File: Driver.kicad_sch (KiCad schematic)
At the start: 41 parts, among them U3 IS31FL3741A

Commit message: Schematic done, partially routed
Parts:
- removed R21, R22, R23, R24, R25, R26, R27, R28, R29, R30, R31, R32, R33, R34, R35, R36, R37, R38, R39, R40, R41, R42, R43, R44, R45: 20, symbol Device:R_US
- removed U3: IS31FL3741A, symbol LEDMatrix:IS31FL3741A
- added U3: IS31FL3729-QFLS4-TR, Package_DFN_QFN:Texas_RSN_WQFN-32-1EP_4x4mm_P0.4mm_EP2.8x2.8mm_ThermalVias, symbol LEDMatrix:IS31FL3729
- C17, C19, C21: footprint (none) -> Capacitor_SMD:C_0402_1005Metric; Digikey (none) -> 1276-1445-1-ND; LCSC (none) -> C52923
- C18, C20, C22: footprint (none) -> Capacitor_SMD:C_0402_1005Metric; Digikey (none) -> 1276-1001-1-ND; LCSC (none) -> C1525
- R12: value 100k -> 18k; footprint (none) -> Resistor_SMD:R_0402_1005Metric
- R13, R14, R15, R16, R17, R18, R19, R20: footprint (none) -> Resistor_SMD:R_0402_1005Metric
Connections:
- net +5V: now also U3.23 (PVCC)
- net GND: now also U3.24 (GND), U3.28 (ADDR), U3.9 (GND), U3.PAD (GND)
- net LED_SW0: now also U3.22 (SW1)
- net LED_SW1: now also U3.21 (SW2)
- net LED_SW2: now also U3.20 (SW3)
- net LED_SW3: now also U3.19 (SW4)
- net LED_SW4: now also U3.18 (SW5)
- net LED_SW5: now also U3.17 (SW6)
- net LED_SW6: now also U3.16 (SW7)
- net LED_SW7: now also U3.15 (SW8)
- net LED_SW8: now also U3.14 (SW9/CS16)
- net SCL: now also U3.27 (SCL)
- net SDA: now also U3.26 (SDA)
- net SDB: now also U3.29 (SDB)
- net at R12.1: now also U3.25 (ISET)
- net at R18.1: now also U3.3 (CS6)
- net at R20.1: now also U3.5 (CS8)
- net at R13.1: now also U3.30 (CS1)
- net at R16.1: now also U3.1 (CS4)
- net at R17.1: now also U3.2 (CS5)
- net at R14.1: now also U3.31 (CS2)
- net at R15.1: now also U3.32 (CS3)
- net at R19.1: now also U3.4 (CS7)
- no-connect marks 6 -> 7
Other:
- moved on the sheet: R12

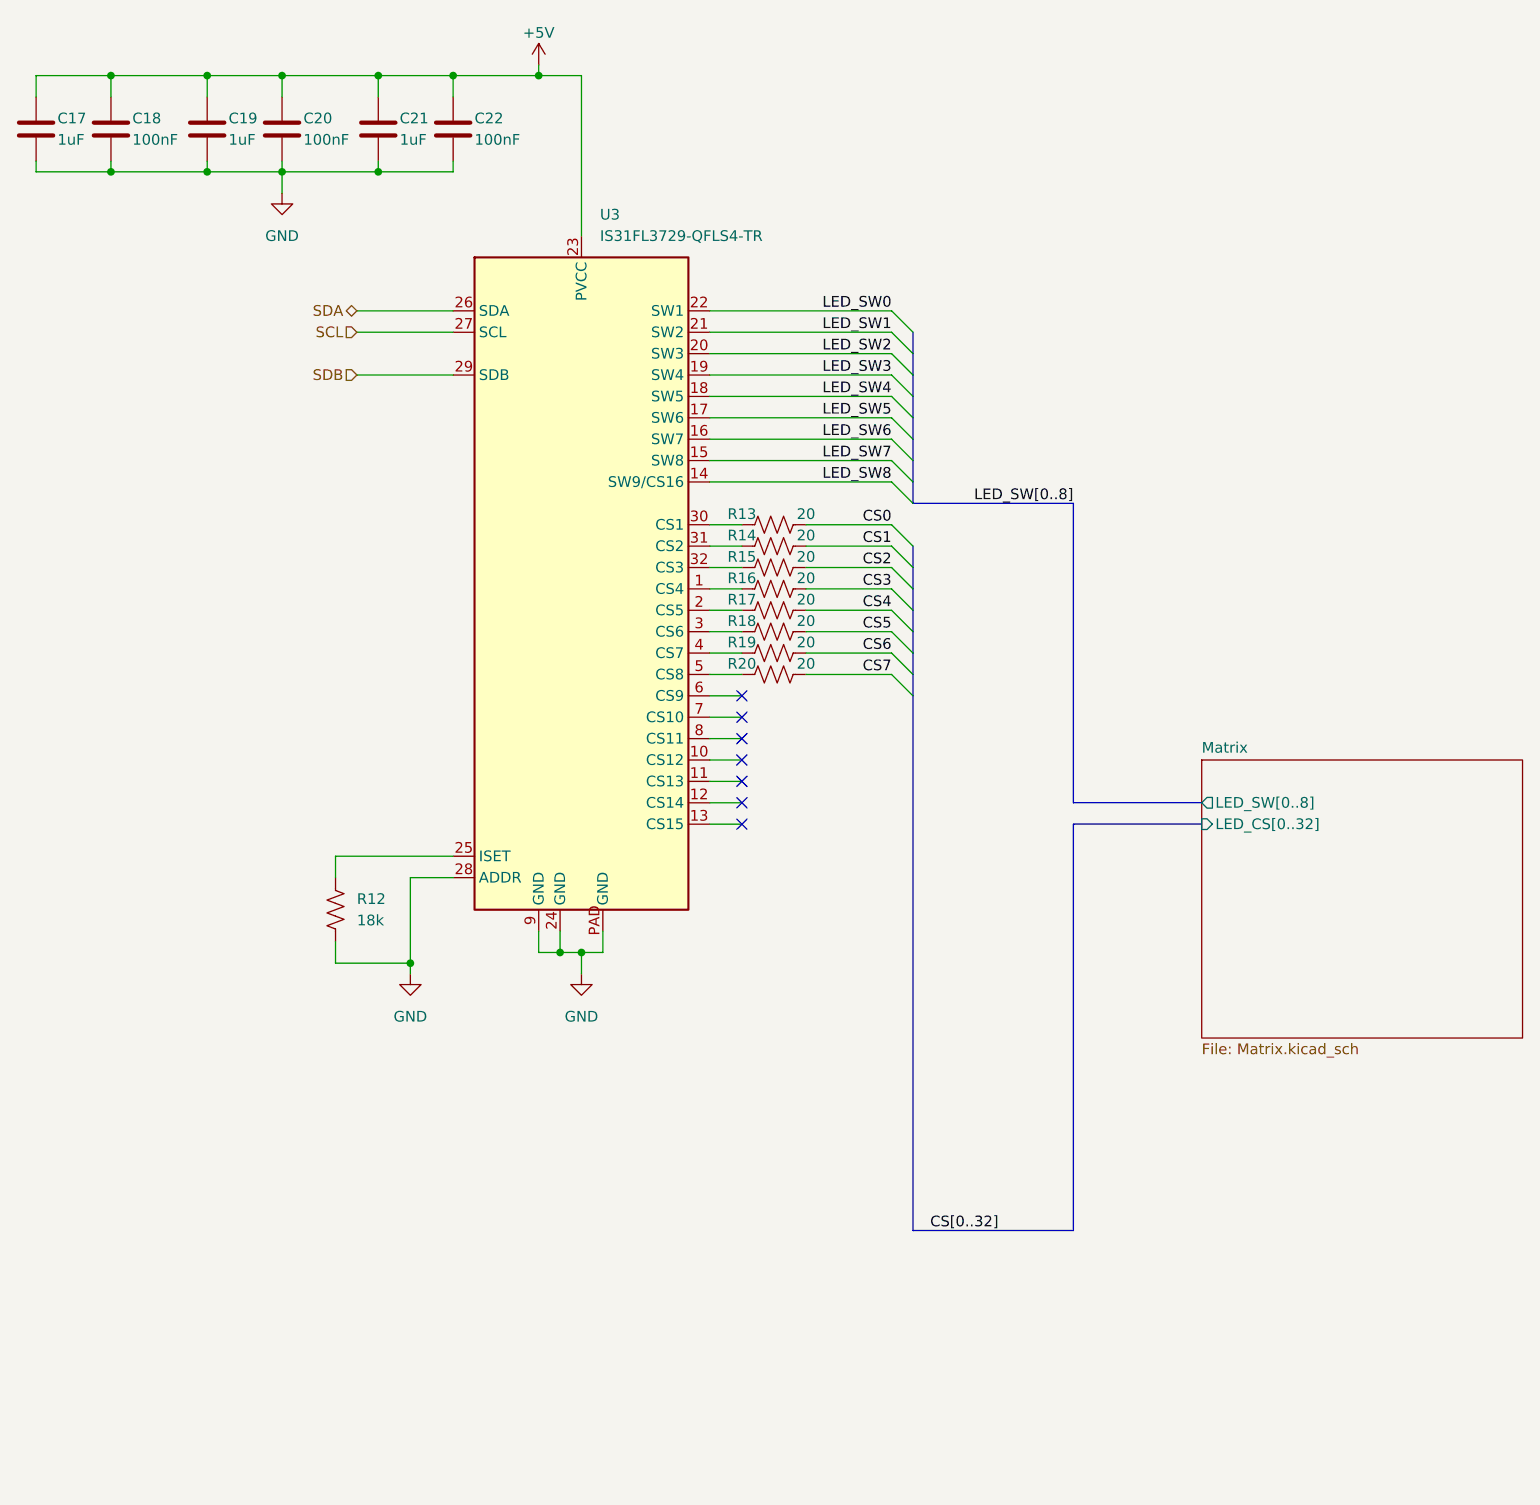
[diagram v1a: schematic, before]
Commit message: Routing complete but not DRC clean
Also want to add 3-9 neopixels here to backlight the legend.
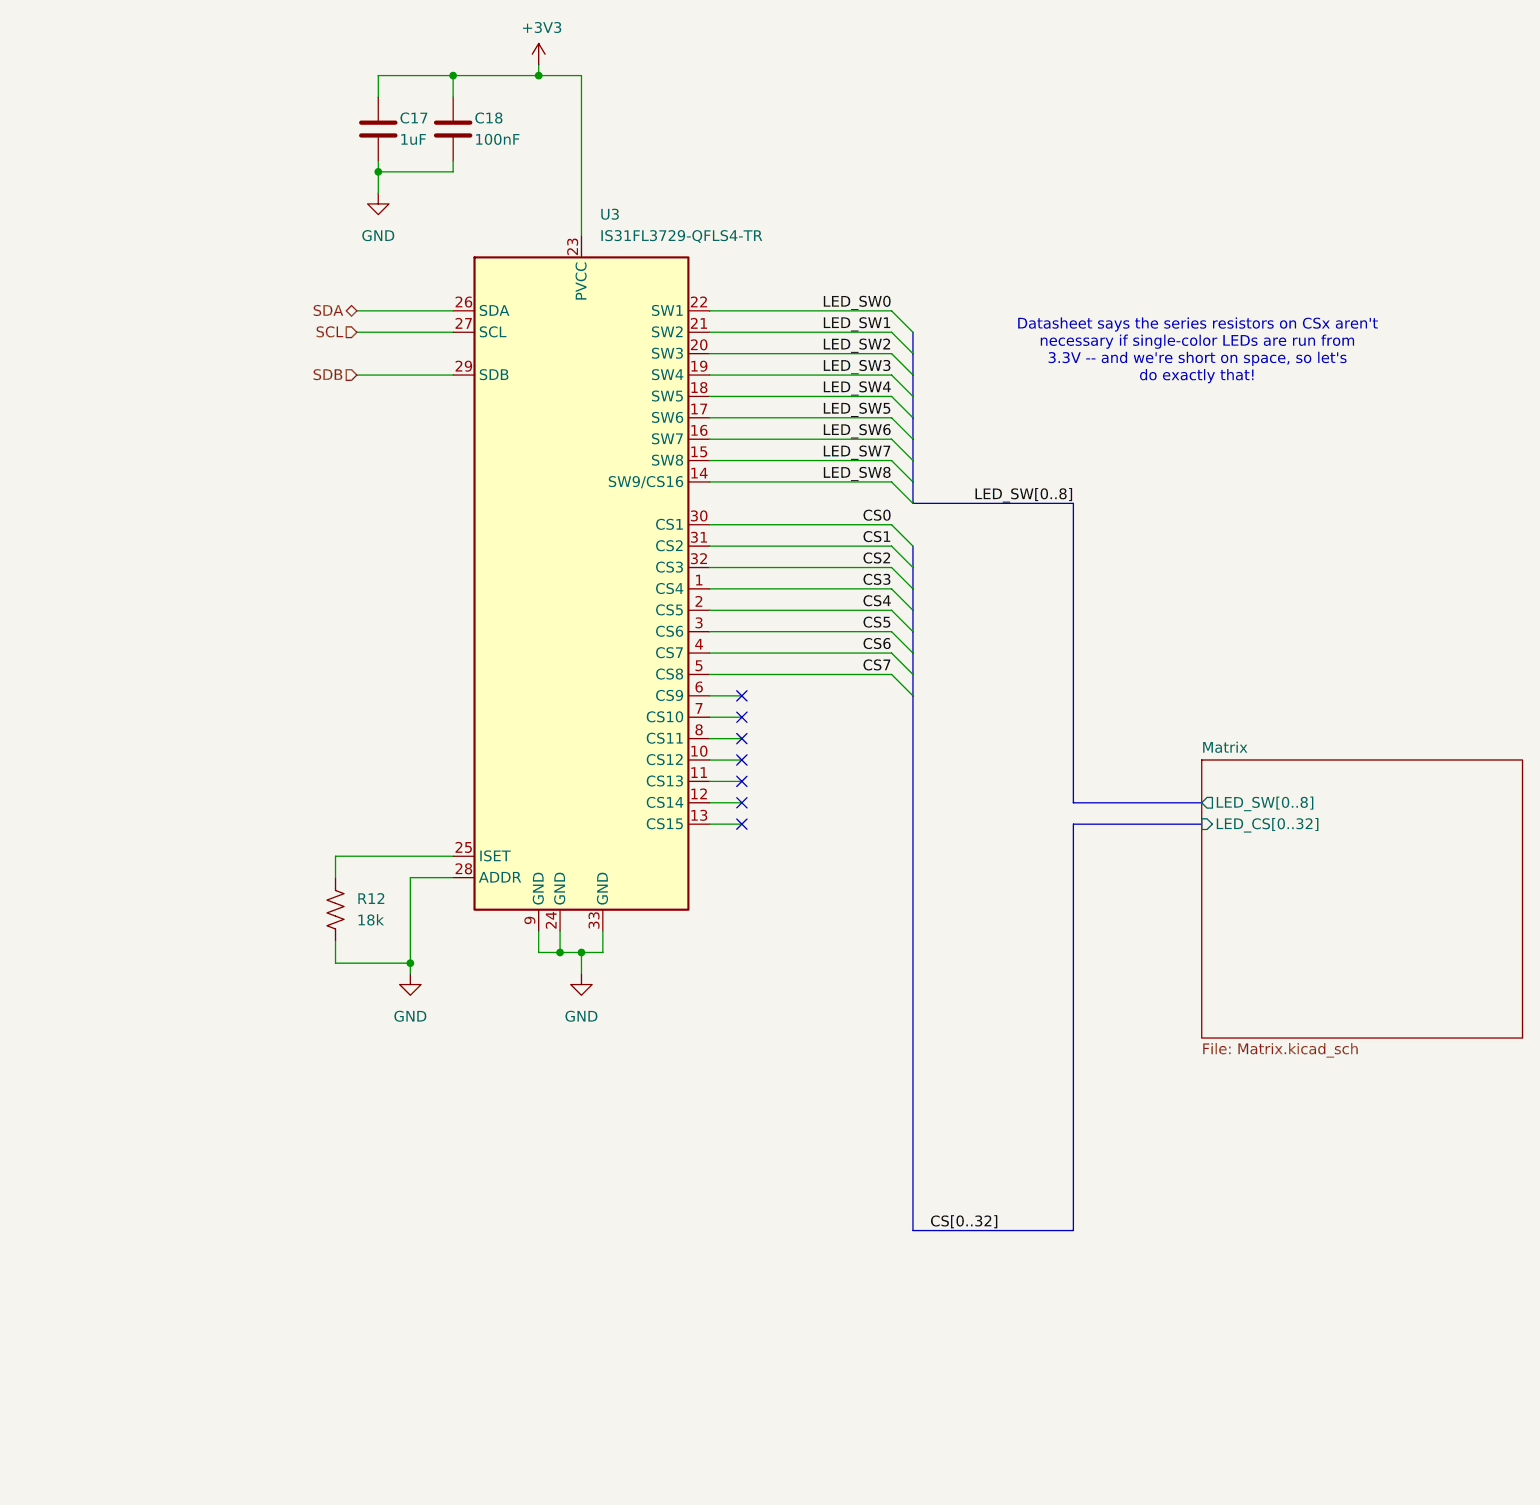
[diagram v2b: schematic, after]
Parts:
- removed C19, C21: 1uF, Capacitor_SMD:C_0402_1005Metric, symbol Device:C
- removed C20, C22: 100nF, Capacitor_SMD:C_0402_1005Metric, symbol Device:C
- removed R13, R14, R15, R16, R17, R18, R19, R20: 20, Resistor_SMD:R_0402_1005Metric, symbol Device:R_US
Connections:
- net CS0: now also U3.30 (CS1)
- net CS1: now also U3.31 (CS2)
- net CS2: now also U3.32 (CS3)
- net CS3: now also U3.1 (CS4)
- net CS4: now also U3.2 (CS5)
- net CS5: now also U3.3 (CS6)
- net CS6: now also U3.4 (CS7)
- net CS7: now also U3.5 (CS8)
- net GND: now also U3.33 (GND); no longer U3.PAD (GND)
- net +5V renamed +3V3
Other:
- note added: "Datasheet says the series resistors on CSx aren't necessary if single-color LEDs are run from 3.3V -- and we're short on space, so let's do exactly that!"
- moved on the sheet: C17, C18

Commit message: Finished version w/ legend on silkscreen, DRC clean
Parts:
- R12: LCSC (none) -> C25762
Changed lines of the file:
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@@
+			)
+		)
+		(property "LCSC" "C25762"
+			(at 57.15 120.65 0)
+			(effects
+				(font
+					(size 1.27 1.27)
+				)
+				(hide yes)
 			)
 		)

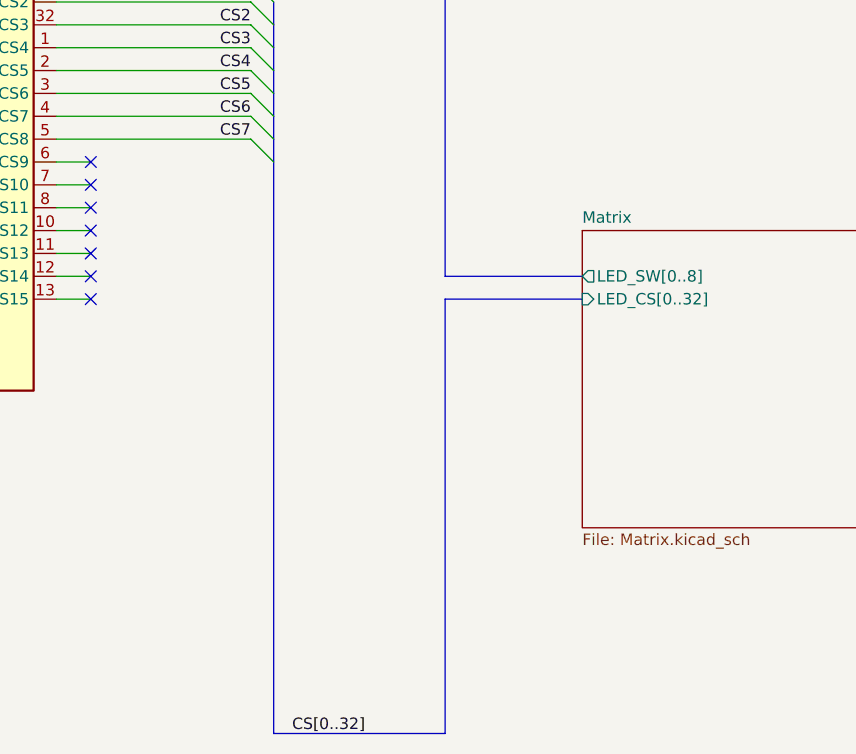
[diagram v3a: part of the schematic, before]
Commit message: Version 2, with right angle neopixel backlighting
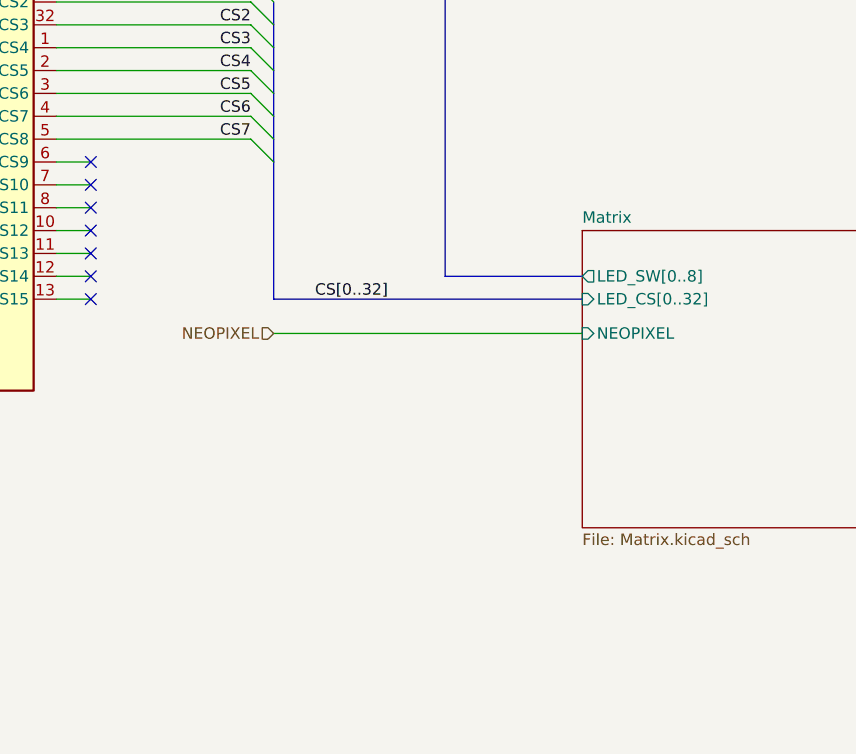
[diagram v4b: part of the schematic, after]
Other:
- sheet Matrix ports: added NEOPIXEL; removed none

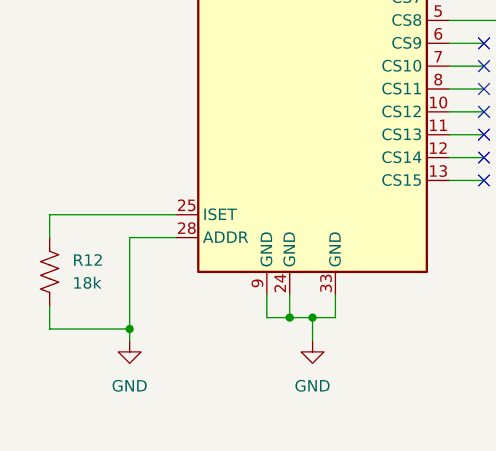
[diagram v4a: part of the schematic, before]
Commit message: Another update before sending to JLCPCB
1. Narrowed the spacing between the LED displays
2. Made the position of the neopixels more consistent
3. Extended the silkscreen up a bit
4. Added my name to the front of the board
5. Designed the enclosure grid
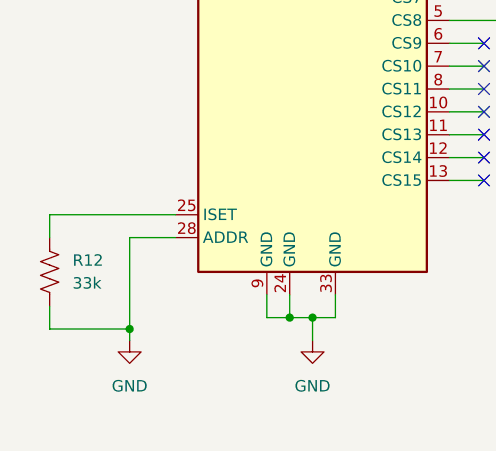
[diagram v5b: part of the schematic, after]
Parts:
- R12: value 18k -> 33k; LCSC C25762 -> C25779
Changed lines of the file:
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@@
 			)
 		)
-		(property "Value" "18k"
+		(property "Value" "33k"
 			(at 59.69 121.9199 0)
 			(effects
@@
 			)
 		)
-		(property "LCSC" "C25762"
+		(property "LCSC" "C25779"
+			(at 57.15 120.65 0)
+			(effects
+				(font
+					(size 1.27 1.27)
+				)
+				(hide yes)
+			)
+		)
+		(property "JLCPCB Position Offset" ""
+			(at 57.15 120.65 0)
+			(effects
+				(font
+					(size 1.27 1.27)
+				)
+				(hide yes)
+			)
+		)
+		(property "JLCPCB Rotation Offset" ""
 			(at 57.15 120.65 0)
 			(effects
@@
 		)
 		(property "LCSC" "C1525"
+			(at 71.12 27.94 0)
+			(effects
+				(font
+					(size 1.27 1.27)
+				)
+				(hide yes)
+			)
+		)
+		(property "JLCPCB Position Offset" ""
+			(at 71.12 27.94 0)
+			(effects
+				(font
+					(size 1.27 1.27)
+				)
+				(hide yes)
+			)
+		)
+		(property "JLCPCB Rotation Offset" ""
 			(at 71.12 27.94 0)
 			(effects
@@
 			)
 		)
+		(property "JLCPCB Position Offset" ""
+			(at 62.23 27.94 0)
+			(effects
+				(font
+					(size 1.27 1.27)
+				)
+				(hide yes)
+			)
+		)
+		(property "JLCPCB Rotation Offset" ""
+			(at 62.23 27.94 0)
+			(effects
+				(font
+					(size 1.27 1.27)
+				)
+				(hide yes)
+			)
+		)
 		(pin "1"
 		)
@@
 			(at 86.36 109.22 0)
 			(effects
+				(font
+					(size 1.27 1.27)
+				)
+				(hide yes)
+			)
+		)
+		(property "JLCPCB Position Offset" ""
+			(at 86.36 109.22 0)
+			(effects
+				(font
+					(size 1.27 1.27)
+				)
+				(hide yes)
+			)
+		)
+		(property "JLCPCB Rotation Offset" ""
+			(at 86.36 109.22 0)
+			(effects
